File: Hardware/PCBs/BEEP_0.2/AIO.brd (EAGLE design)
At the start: 106 x 69.1 mm, 90 parts, among them IC1 74HC238SSOP, IC2 74HC238SSOP, IC3 ULN2803ASOP18, IC4 ULN2803ASOP18, IC5 TS34119SMD, Q1 DMN2075U, Q2 DMN2075U, Q3 DMN2075U, Q4 DMN2075U, Q5 DMN2075U, Q6 32Mhz, U1 ATXMEGA64D3-AU, U2 TB6612FNG, X1 Sens1, X10 exp header, X11 MICROMATCH-10, X12 MICROMATCH-4, X13 MICROMATCH-4, X2 Sens2, X3 MICROMATCH-8, X4 MICROMATCH-8, X5 PDI interface (ISP), X6 Sens5, X7 Sens6, X8 MICROMATCH-8, X9 MICROMATCH-8

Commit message: minor enhancements
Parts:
- removed U1: ATXMEGA64D3-AU, atmel-xmega:TQFP-64A-64
- added IC8: TS34119SMD, BEEP:SO08
- C10, C15: value 1uF -> 100nF
- C11: value 10uF -> 100nF; device rcl:SMC_D -> rcl:C0603
- C12: value 10uF -> 1uF; device rcl:SMC_D -> rcl:C0603
- C13, C14: value 100nF -> 10uF; device rcl:C0603 -> rcl:SMC_D
- C16: value 22pF -> 100nF
- C17: value 22pF -> 1uF
- C7, C8: value 100nF -> 22pF
- IC5: value TS34119SMD -> ATXMEGA64D3-AU; device BEEP:SO08 -> atmel-xmega:TQFP-64A-64
- Q4: value DMN2075U -> 32Mhz; device BEEP:SOT95P240X112-3N -> crystal:HC49/S
- Q6: value 32Mhz -> DMN2075U; device crystal:HC49/S -> BEEP:SOT95P240X112-3N
- R11: value 10k -> 100R
- R12: value 220R -> 10k
- R13: value 390R -> 220R
- R14: value 100R -> 390R
- R15: value (none) -> 100R
- R16: device rcl:R0603 -> resistor:M0805
- R17: value 3k -> (none); device rcl:R0603 -> resistor:M0805
- R18: value 75k -> 3k
- R19: value 1K -> 75k
- R20: value 10k -> 1K
- R21: value 100k -> (none); device rcl:R0603 -> resistor:M0805
- R22, R25, R26, R28, R29, R4, R5, R6: device rcl:R0805 -> resistor:M0805
- R23, R30: value (none) -> 10k; device rcl:R0805 -> rcl:R0603
- R24: value 10k -> 100k
- R27: value (none) -> 0R; device rcl:R0805 -> rcl:R0603
- R31: value 0R -> (none); device rcl:R0603 -> resistor:M0805
- R32: value 100R -> (none); device rcl:R0603 -> resistor:M0805
- R8, R9: device rcl:R0603 -> rcl:M0805
- moved R19 71.9 mm to (68.9, 18.9), turned to 270 degrees
- moved R15 66.0 mm to (7.13, 24.9), turned to 270 degrees
- moved R25 61.7 mm to (29.2, 9.02), turned to 90 degrees
- moved R26 61.7 mm to (39.4, 69.9), turned to 270 degrees
- moved Q4 59.5 mm to (59.4, 57.5), turned to 270 degrees
- moved Q6 59.5 mm to (10.9, 23.0), turned to 0 degrees
- moved R14 59.5 mm to (46.7, 69.4), turned to 90 degrees
- moved C17 53.5 mm to (43.5, 14.1)
- moved R27 52.8 mm to (35.3, 28.8)
- moved C9 49.4 mm to (33.6, 57.6), turned to 270 degrees
- moved R20 49.3 mm to (3.89, 49.7), turned to 90 degrees
- moved C12 44.7 mm to (71.1, 18.9), turned to 90 degrees
- moved IC5 44.3 mm to (46.3, 55.9), turned to 270 degrees
- moved C16 42.2 mm to (25.8, 27.1), turned to 0 degrees
- moved R32 40.5 mm to (67.3, 66.4), turned to 270 degrees
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- renumbered U$10 to D1, U$11 to D4, U$12 to D3, U$5 to IC6, U$7 to IC9, U$8 to Q7, U$9 to D2, U2 to IC7
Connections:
- net +3V3: now also C10.2, C13.-, C15.2, C9.2, IC5.15, IC5.25, IC5.35, IC5.45, IC5.53, IC5.61, R12.1; no longer C11.-, C13.2, C7.2, C8.2, R11.1, U1.15, U1.25, U1.35, U1.45, U1.53, U1.61
- net +5V: now also IC8.6, R31.2, R32.2; no longer IC5.6, R29.2, R30.2
- net +7V: now also C14.-, C16.2, R16.1, R27.2, R30.1; no longer C12.-, C14.2, R15.1, R24.1, R31.2
- net ADISTANCE_0: now also IC5.6; no longer U1.6
- net ADISTANCE_1: now also IC5.7; no longer U1.7
- net ADISTANCE_2: now also IC5.8; no longer U1.8
- net ADISTANCE_3: now also IC5.9; no longer U1.9
- net ADISTANCE_4: now also IC5.10; no longer U1.10
- net ADISTANCE_5: now also IC5.11; no longer U1.11
- net ADISTANCE_6: now also IC5.12; no longer U1.12
- net ADISTANCE_7: now also IC5.13; no longer U1.13
- net AUDIO_DISABLE: now also IC5.54, IC8.1; no longer IC5.1, U1.54
- net AUDIO_IN: now also C11.2; no longer C9.2
- net BATT_GND: now also Q6.D; no longer Q4.D
- net BATT_U: now also R15.1, R23.1, R27.1; no longer R14.1, R20.1, R31.1
- net BATT_VOLTAGE: now also IC5.64, R16.2, R17.1; no longer R15.2, R16.1, U1.64
- net BATT_WARN_0: now also IC5.1, R13.1; no longer R12.1, U1.1
- net BATT_WARN_1: now also IC5.2, R14.1; no longer R13.1, U1.2
- net COLOR_DIODE_1: now also IC5.31; no longer U1.31
- net COLOR_DIODE_2: now also IC5.32; no longer U1.32
- net COLOR_FREQ_OUT: now also IC5.26; no longer U1.26
- net COLOR_SENSOR_1: now also IC5.33; no longer U1.33
- net COLOR_SENSOR_2: now also IC5.27; no longer U1.27
- net COLOR_SENSOR_3: now also IC5.30; no longer U1.30
- net COLOR_SENSOR_PWM_LED: now also IC5.39, R11.1; no longer R32.1, U1.39
- net ENCODER_L2: now also R29.2; no longer R27.2
- net ENCODER_R1: now also R21.2; no longer R23.2
- net GND: now also C10.1, C12.2, C13.+, C14.+, C15.1, C17.2, C9.1, IC5.14, IC5.24, IC5.34, IC5.44, IC5.52, IC5.60, IC5.63, IC8.7, Q6.S, R17.2, R20.2, R21.1, R29.1; no longer C10.2, C11.+, C12.+, C13.1, C14.1, C15.2, C17.1, IC5.7, Q4.S, R16.2, R19.2, R23.1, R27.1, U1.14, U1.24, U1.34, U1.44, U1.52, U1.60, U1.63
- net IR_LED_MK0: now also IC5.46; no longer U1.46
- net IR_LED_MK1: now also IC5.47; no longer U1.47
- net IR_LED_MK2: now also IC5.48; no longer U1.48
- net LED_A0: now also IC5.36; no longer U1.36
- net LED_A1: now also IC5.37; no longer U1.37
- net LED_A2: now also IC5.38; no longer U1.38
- net MOTOR_A_IN1: now also IC5.41; no longer U1.41
- net MOTOR_A_IN2: now also IC5.40; no longer U1.40
- net MOTOR_A_PWM: now also IC5.19; no longer U1.19
- net MOTOR_B_IN1: now also IC5.42; no longer U1.42
- net MOTOR_B_IN2: now also IC5.43; no longer U1.43
- net MOTOR_B_PWM: now also IC5.18; no longer U1.18
- net MOTOR_STBY: now also IC5.22; no longer U1.22
- net N$11: now also R32.1; no longer R29.1
- net N$14: now also C8.2, IC5.59, Q4.1; no longer C17.2, Q6.1, U1.59
- net N$15: now also IC8.4, R18.1, R19.2; no longer IC5.4, R17.1, R18.2
- net N$16: now also C17.1, R24.2; no longer C15.1, R21.2
- net N$17: now also C11.1, R18.2; no longer C9.1, R17.2
- net N$18: now also C7.2, IC5.58, Q4.2; no longer C16.2, Q6.2, U1.58
- net N$19: now also R20.1; no longer R19.1
- net N$20: now also R25.1; no longer R26.1
- net N$22: now also R23.2, R24.1; no longer R20.2, R21.1
- net N$23: now also R26.1; no longer R25.1
- net N$25: now also R11.2; no longer R32.2
- net N$26: now also R31.1; no longer R30.1
- net N$29: now also R14.2; no longer R13.2
- net N$32: now also R13.2; no longer R12.2
- net N$36: now also C12.1, IC8.2; no longer C10.1, IC5.2
- net N$4: now also IC5.62; no longer U1.62
- net N$8: now also Q6.G, R15.2; no longer Q4.G, R14.2
- net PDI_CLK: now also IC5.57; no longer U1.57
- net PDI_DATA: now also IC5.56; no longer U1.56
- net POWER_OFF: now also IC5.23, R30.2; no longer R24.2, U1.23
- net RGB_LED_MK0: now also IC5.51; no longer U1.51
- net RGB_LED_MK1: now also IC5.50; no longer U1.50
- net RGB_LED_MK2: now also IC5.49; no longer U1.49
- net RPI_RX: now also IC5.29; no longer U1.29
- net RPI_TX: now also IC5.28; no longer U1.28
- net SCL: now also IC5.17, R12.2; no longer R11.2, U1.17
- net SDA: now also IC5.16; no longer U1.16
- net SPEAKER_O1: now also IC8.8; no longer IC5.8
- net SPEAKER_O2: now also IC8.5, R19.1; no longer IC5.5, R18.1
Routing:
- net GND: track 674.6 -> 677.3 mm
- net +3V3: track 411.5 -> 409.9 mm
- net N$4: track 26.3 -> 25.5 mm

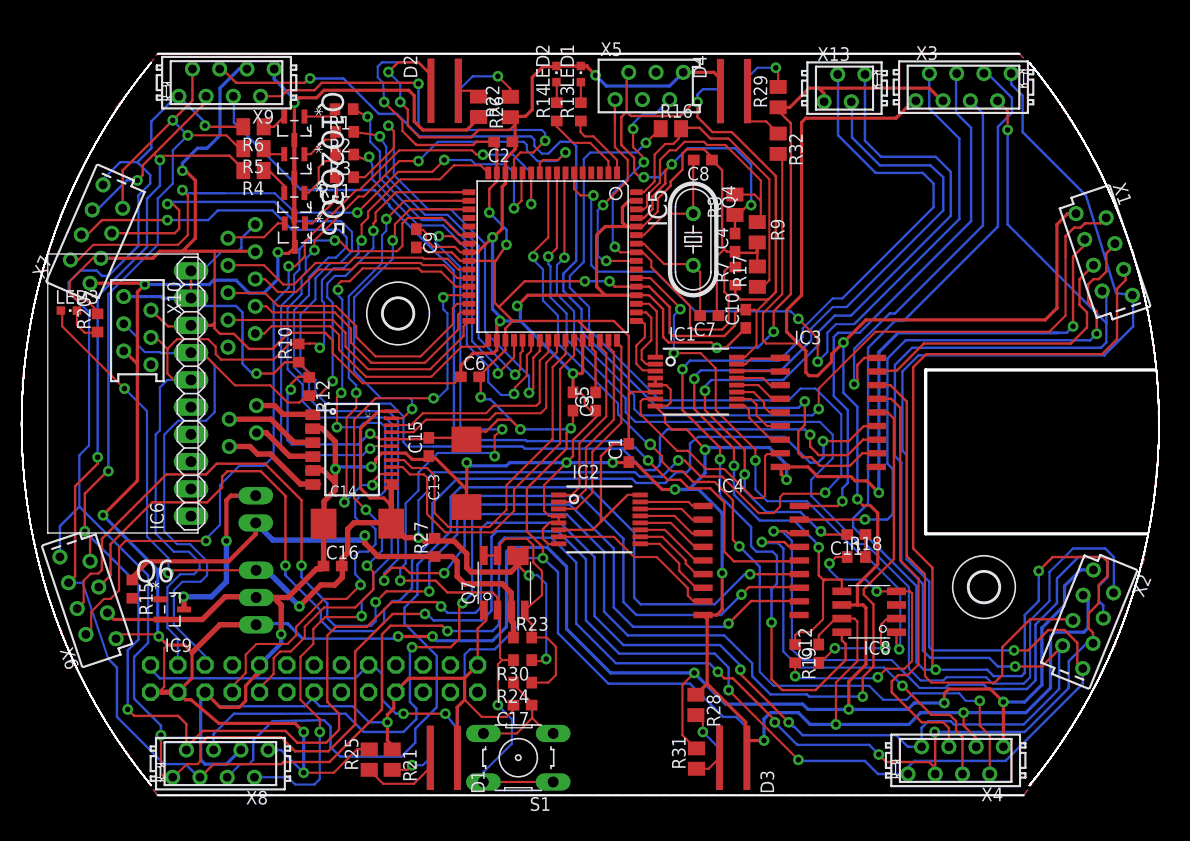
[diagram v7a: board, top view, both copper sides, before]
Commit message: add 3M 8526-4500PL to RPi drawing and adjust PCB change keepout to restrict layer for usb and network port locations
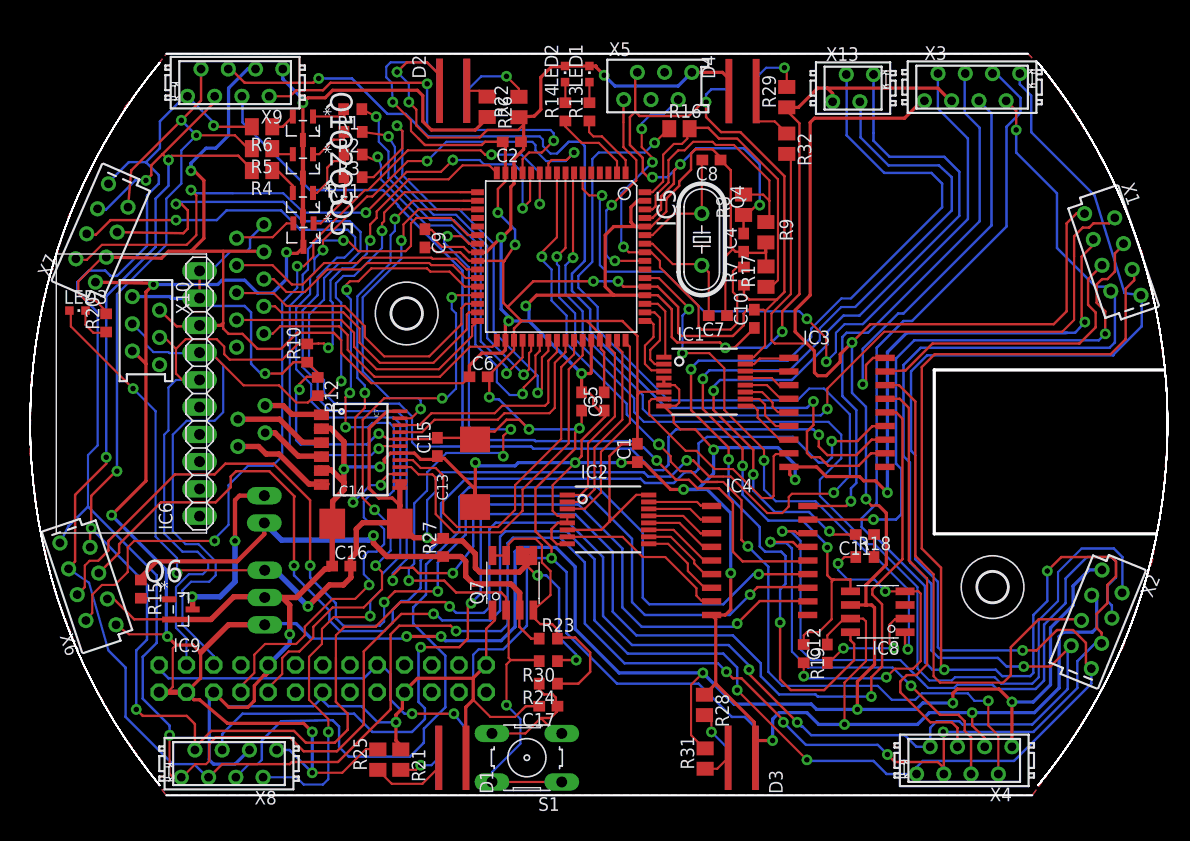
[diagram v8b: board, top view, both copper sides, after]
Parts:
- moved C17 2.40 mm to (45.9, 14.0)
- moved R23 2.40 mm to (45.9, 20.3)
- moved R24 2.40 mm to (45.9, 16.1)
- moved R30 2.40 mm to (45.9, 18.2)
- moved X6 1.30 mm to (3.00, 25.4)
- moved C11 0.80 mm to (75.4, 30.0)
- moved C12 0.80 mm to (71.9, 18.9)
- moved IC3 0.80 mm to (72.8, 41.4)
- moved R17 0.80 mm to (66.2, 54.0)
- moved R18 0.80 mm to (75.4, 27.9)
- moved R29 0.80 mm to (68.1, 70.8)
- moved R32 0.80 mm to (68.1, 66.4)
- moved C1 0.80 mm to (54.2, 37.6)
- moved C15 0.80 mm to (35.6, 38.2)
- moved C5 0.80 mm to (51.1, 42.4)
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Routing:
- net LED_A1_OUT: track 310.1 -> 306.4 mm
- net GND: track 677.3 -> 680.6 mm
- net N$22: track 24.1 -> 27.2 mm
- net POWER_OFF: track 84.0 -> 85.7 mm
- net N$16: track 11.7 -> 13.2 mm
- net +5V: track 408.6 -> 410.0 mm
- net +7V: track 216.1 -> 217.3 mm
- net BATT_U: track 46.8 -> 48.0 mm
- net LED_A0_OUT: track 314.6 -> 313.5 mm
- net LED_K5_OUT: track 107.1 -> 106.1 mm
- net IR_LED_K5_OUT: track 105.7 -> 104.8 mm
- net ADISTANCE_5: track 82.8 -> 82.2 mm
- net LED_A2_OUT: track 373.8 -> 374.3 mm
